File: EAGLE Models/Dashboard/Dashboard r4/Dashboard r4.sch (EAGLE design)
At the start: 116 parts, among them IC1 AT90CAN128, IC2 MCP2551SO8, IC3 NUP2105L, IC4 FT801, IC5 FT232RL, IC6 LP5907-3.3, IC7 LM5000, IC8 NCP1117, J1 1734753-1_MINIUSB_CON, J2 EN3C12M26X, J3 043650-0409, J4 043650-0409, J5 043650-0409, Q1 56P2859, Q2 MMBT4401-7-F, Q3 MMBT4403-7-F, Q4 MMBT4401-7-F, Q5 MMBT4403-7-F, Q6 MMBT4401-7-F, Q7 MMBT4403-7-F, U1 74LCX125M

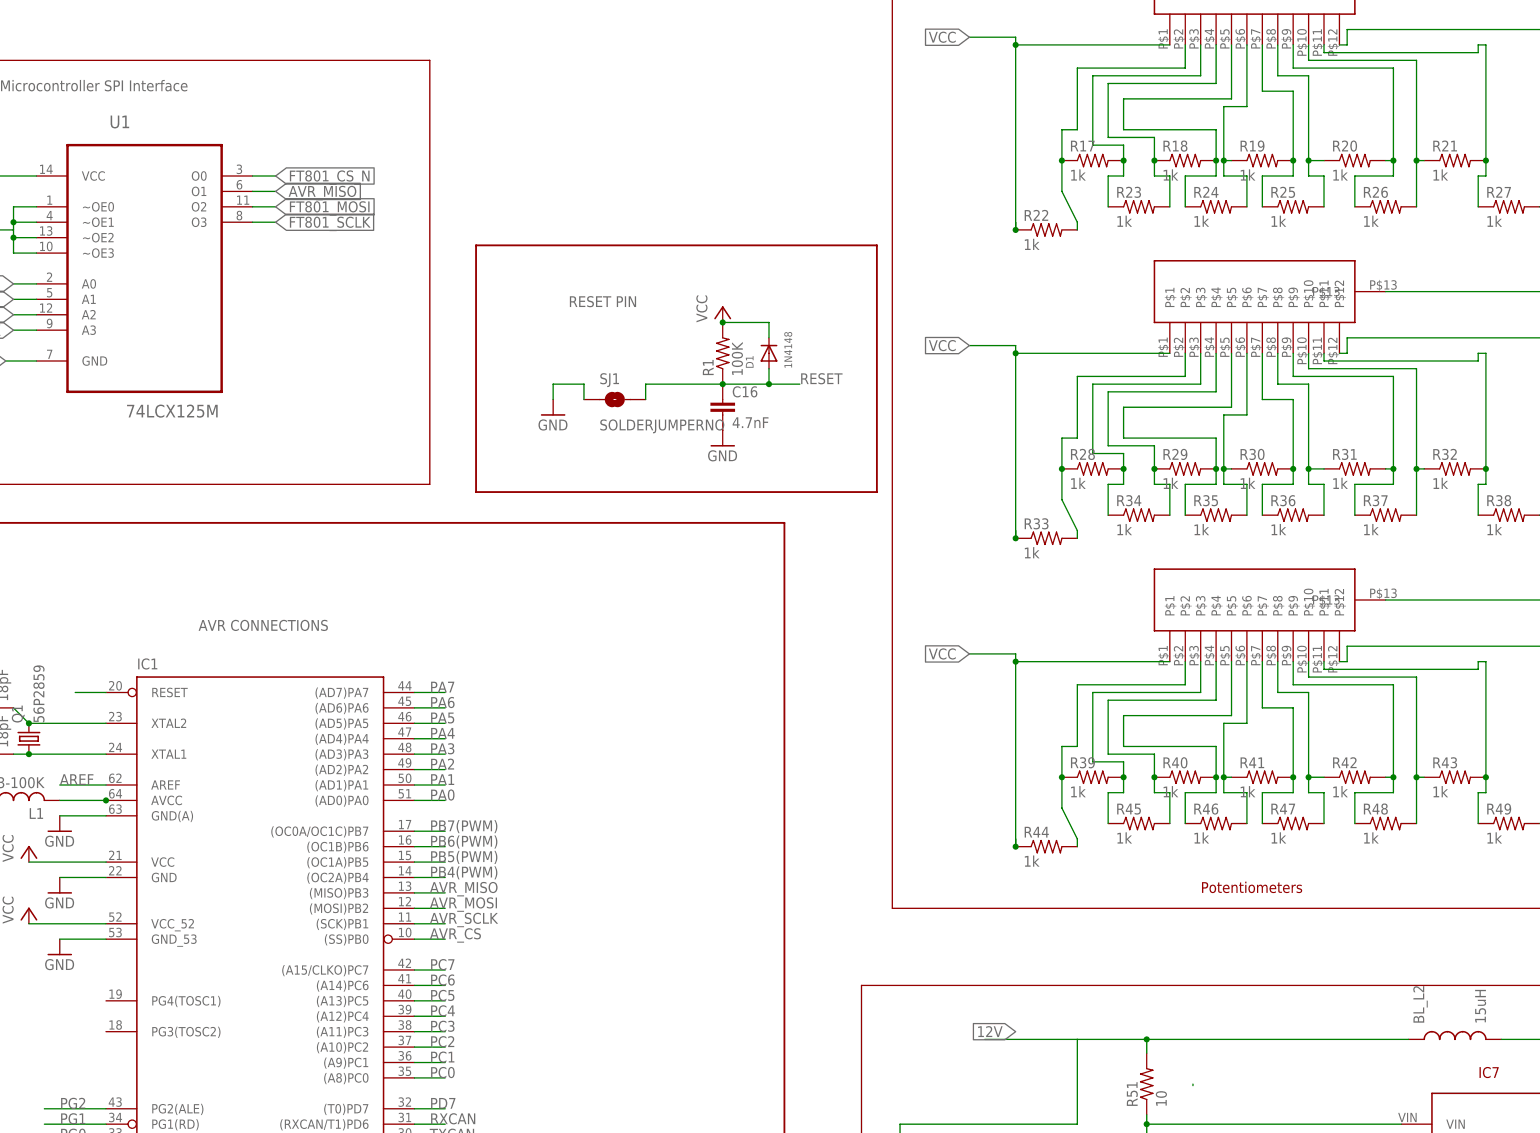
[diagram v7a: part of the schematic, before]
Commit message: Reference designator formatting
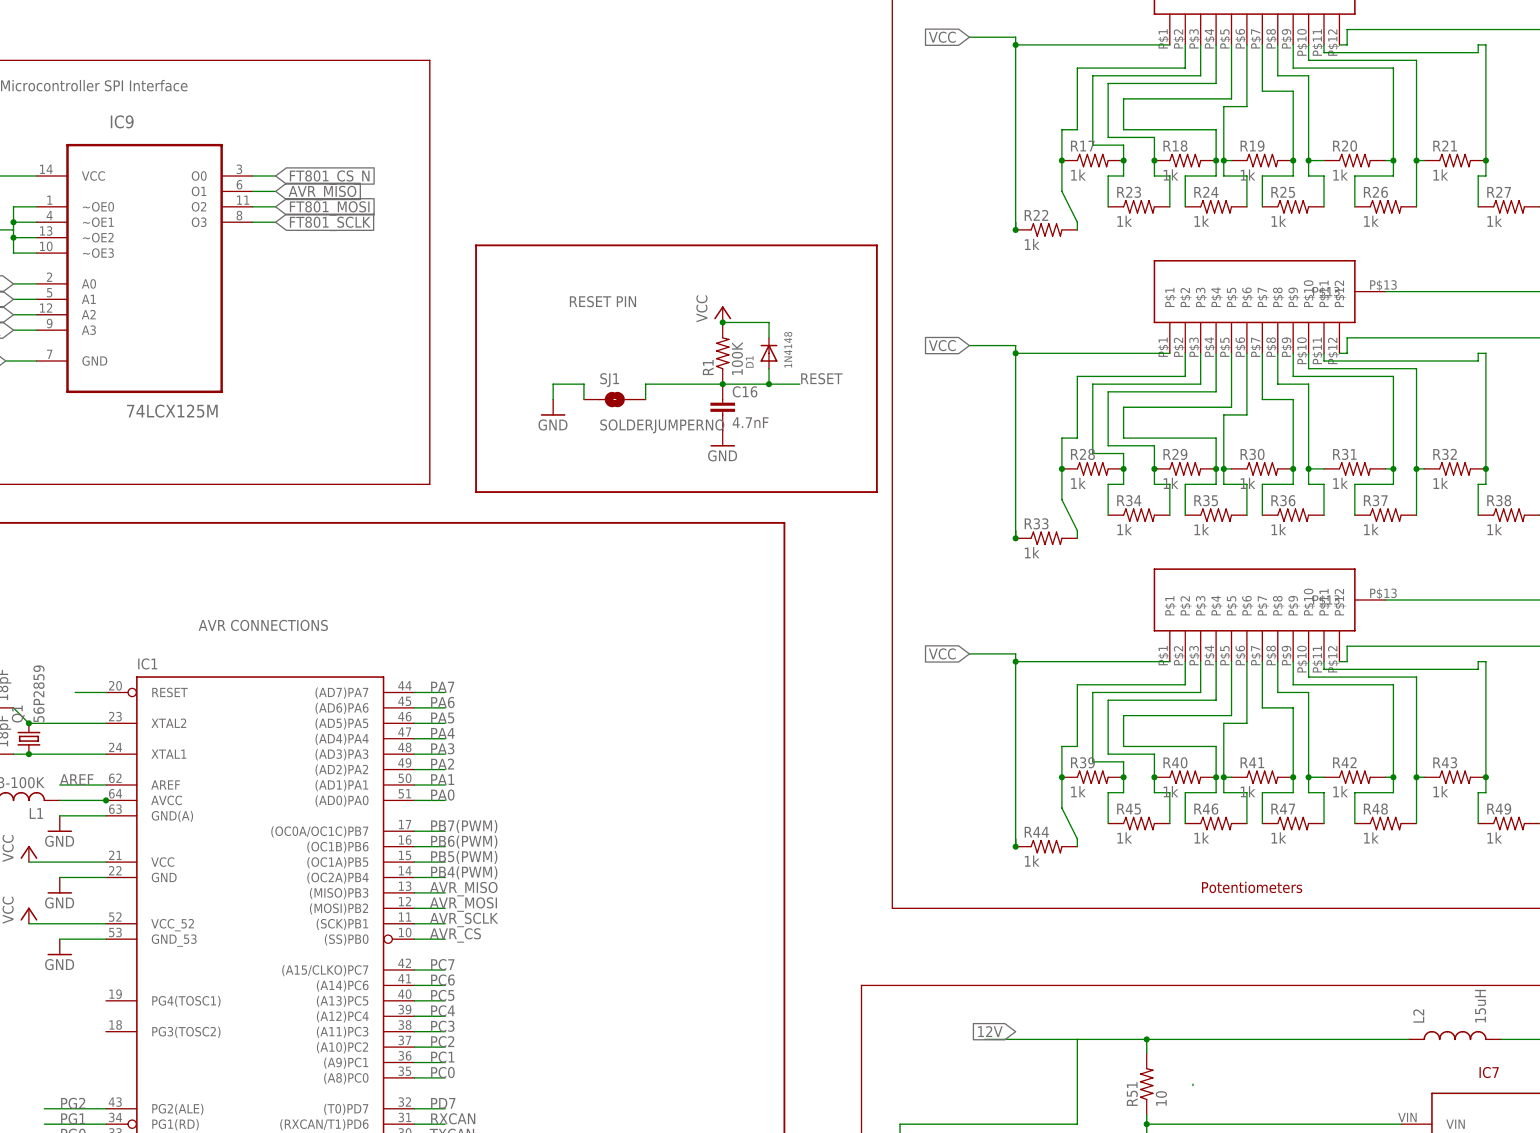
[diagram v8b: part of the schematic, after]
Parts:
- renumbered BL_L2 to L2, U1 to IC9
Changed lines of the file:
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@@
 <?xml version="1.0" encoding="utf-8"?>
 <!DOCTYPE eagle SYSTEM "eagle.dtd">
-<eagle version="8.4.0">
+<eagle version="8.3.2">
 <drawing>
 <settings>
@@
 <part name="GND3" library="SparkFun-Aesthetics" deviceset="GND" device=""/>
 <part name="P+6" library="supply1" library_urn="urn:adsk.eagle:library:371" deviceset="VCC" device=""/>
-<part name="U1" library="Fairchild_By_element14_Batch_1" deviceset="74LCX125M" device=""/>
+<part name="IC9" library="Fairchild_By_element14_Batch_1" deviceset="74LCX125M" device=""/>
 <part name="GND13" library="SparkFun-Aesthetics" deviceset="GND" device=""/>
 <part name="R10" library="SparkFun-Resistors" deviceset="RESISTOR" device="0603" value="47k"/>
@@
 <part name="C6" library="SparkFun-Capacitors" deviceset="CAP" device="0805" value="10uF"/>
 <part name="C17" library="SparkFun-Capacitors" deviceset="CAP" device="0805" value="0.1uF"/>
-<part name="BL_L2" library="tdk" deviceset="LTF4022-D" device="" value="15uH"/>
+<part name="L2" library="tdk" deviceset="LTF4022-D" device="" value="15uH"/>
 <part name="GND21" library="SparkFun-Aesthetics" deviceset="GND" device=""/>
 <part name="C21" library="SparkFun-Capacitors" deviceset="CAP" device="0805" value="100 pF"/>
@@
 <instance part="GND3" gate="1" x="-198.12" y="22.86"/>
 <instance part="P+6" gate="VCC" x="-240.03" y="36.83" rot="R90"/>
-<instance part="U1" gate="A" x="-69.85" y="247.65"/>
+<instance part="IC9" gate="A" x="-69.85" y="247.65"/>
 <instance part="GND13" gate="1" x="-364.49" y="205.74" rot="R270"/>
 <instance part="R10" gate="G$1" x="-389.89" y="217.17" rot="R90"/>
@@
 <instance part="C6" gate="G$1" x="184.15" y="73.914" rot="R90"/>
 <instance part="C17" gate="G$1" x="183.896" y="68.58" rot="R90"/>
-<instance part="BL_L2" gate="A" x="146.05" y="118.11" rot="R90"/>
+<instance part="L2" gate="A" x="146.05" y="118.11" rot="R90"/>
 <instance part="GND21" gate="1" x="119.38" y="60.96"/>
 <instance part="C21" gate="G$1" x="124.714" y="88.9" rot="R90"/>
@@
 </segment>
 <segment>
-<pinref part="U1" gate="A" pin="~OE0"/>
+<pinref part="IC9" gate="A" pin="~OE0"/>
 <wire x1="-87.63" y1="255.27" x2="-91.44" y2="255.27" width="0.1524" layer="91"/>
 <wire x1="-91.44" y1="255.27" x2="-91.44" y2="252.73" width="0.1524" layer="91"/>
-<pinref part="U1" gate="A" pin="~OE1"/>
+<pinref part="IC9" gate="A" pin="~OE1"/>
 <wire x1="-91.44" y1="252.73" x2="-91.44" y2="251.46" width="0.1524" layer="91"/>
 <wire x1="-91.44" y1="251.46" x2="-91.44" y2="250.19" width="0.1524" layer="91"/>
 <wire x1="-91.44" y1="250.19" x2="-91.44" y2="247.65" width="0.1524" layer="91"/>
 <wire x1="-87.63" y1="252.73" x2="-91.44" y2="252.73" width="0.1524" layer="91"/>
-<pinref part="U1" gate="A" pin="~OE2"/>
+<pinref part="IC9" gate="A" pin="~OE2"/>
 <wire x1="-87.63" y1="250.19" x2="-91.44" y2="250.19" width="0.1524" layer="91"/>
-<pinref part="U1" gate="A" pin="~OE3"/>
+<pinref part="IC9" gate="A" pin="~OE3"/>
 <wire x1="-87.63" y1="247.65" x2="-91.44" y2="247.65" width="0.1524" layer="91"/>
 <junction x="-91.44" y="252.73"/>
@@
 </segment>
 <segment>
-<pinref part="U1" gate="A" pin="O1"/>
+<pinref part="IC9" gate="A" pin="O1"/>
 <wire x1="-52.07" y1="257.81" x2="-48.26" y2="257.81" width="0.1524" layer="91"/>
 <label x="-48.26" y="257.81" size="1.778" layer="95" xref="yes"/>
@@
 </segment>
 <segment>
-<pinref part="U1" gate="A" pin="A2"/>
+<pinref part="IC9" gate="A" pin="A2"/>
 <wire x1="-87.63" y1="237.49" x2="-91.44" y2="237.49" width="0.1524" layer="91"/>
 <label x="-91.44" y="237.49" size="1.778" layer="95" rot="R180" xref="yes"/>
@@
 <wire x1="95.25" y1="115.824" x2="95.25" y2="118.11" width="0.1524" layer="91"/>
 <junction x="95.25" y="118.11"/>
-<pinref part="BL_L2" gate="A" pin="1"/>
+<pinref part="L2" gate="A" pin="1"/>
 <pinref part="C15" gate="G$1" pin="1"/>
 <junction x="64.77" y="86.36"/>
@@
 </segment>
 <segment>
-<pinref part="U1" gate="A" pin="A0"/>
+<pinref part="IC9" gate="A" pin="A0"/>
 <wire x1="-87.63" y1="242.57" x2="-91.44" y2="242.57" width="0.1524" layer="91"/>
 <label x="-91.44" y="242.57" size="1.778" layer="95" rot="R180" xref="yes"/>
@@
 </segment>
 <segment>
-<pinref part="U1" gate="A" pin="VCC"/>
+<pinref part="IC9" gate="A" pin="VCC"/>
 <wire x1="-87.63" y1="260.35" x2="-93.98" y2="260.35" width="0.1524" layer="91"/>
 <label x="-93.98" y="260.35" size="1.778" layer="95" rot="R180" xref="yes"/>
@@
 </segment>
 <segment>
-<pinref part="U1" gate="A" pin="A1"/>
+<pinref part="IC9" gate="A" pin="A1"/>
 <wire x1="-87.63" y1="240.03" x2="-91.44" y2="240.03" width="0.1524" layer="91"/>
 <label x="-91.44" y="240.03" size="1.778" layer="95" rot="R180" xref="yes"/>
@@
 </segment>
 <segment>
-<pinref part="U1" gate="A" pin="O2"/>
+<pinref part="IC9" gate="A" pin="O2"/>
 <wire x1="-52.07" y1="255.27" x2="-48.26" y2="255.27" width="0.1524" layer="91"/>
 <label x="-48.26" y="255.27" size="1.778" layer="95" xref="yes"/>
@@
 </segment>
 <segment>
-<pinref part="U1" gate="A" pin="O0"/>
+<pinref part="IC9" gate="A" pin="O0"/>
 <wire x1="-52.07" y1="260.35" x2="-48.26" y2="260.35" width="0.1524" layer="91"/>
 <label x="-48.26" y="260.35" size="1.778" layer="95" xref="yes"/>
@@
 </segment>
 <segment>
-<pinref part="U1" gate="A" pin="O3"/>
+<pinref part="IC9" gate="A" pin="O3"/>
 <wire x1="-52.07" y1="252.73" x2="-48.26" y2="252.73" width="0.1524" layer="91"/>
 <label x="-48.26" y="252.73" size="1.778" layer="95" xref="yes"/>
@@
 <net name="N$1" class="2">
 <segment>
-<pinref part="U1" gate="A" pin="GND"/>
+<pinref part="IC9" gate="A" pin="GND"/>
 <wire x1="-87.63" y1="229.87" x2="-92.71" y2="229.87" width="0.1524" layer="91"/>
 <label x="-92.71" y="229.87" size="1.778" layer="95" rot="R180" xref="yes"/>
@@
 <net name="AVR_SCLK" class="0">
 <segment>
-<pinref part="U1" gate="A" pin="A3"/>
+<pinref part="IC9" gate="A" pin="A3"/>
 <wire x1="-87.63" y1="234.95" x2="-91.44" y2="234.95" width="0.1524" layer="91"/>
 <label x="-91.44" y="234.95" size="1.778" layer="95" rot="R180" xref="yes"/>
@@
 <wire x1="172.72" y1="99.06" x2="187.706" y2="99.06" width="0.1524" layer="91"/>
 <junction x="187.706" y="99.06"/>
-<pinref part="BL_L2" gate="A" pin="2"/>
+<pinref part="L2" gate="A" pin="2"/>
 <wire x1="153.67" y1="118.11" x2="187.706" y2="118.11" width="0.1524" layer="91"/>
 <wire x1="187.706" y1="118.11" x2="191.262" y2="118.11" width="0.1524" layer="91"/>
